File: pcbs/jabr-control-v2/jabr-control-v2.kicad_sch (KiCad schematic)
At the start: 4 parts

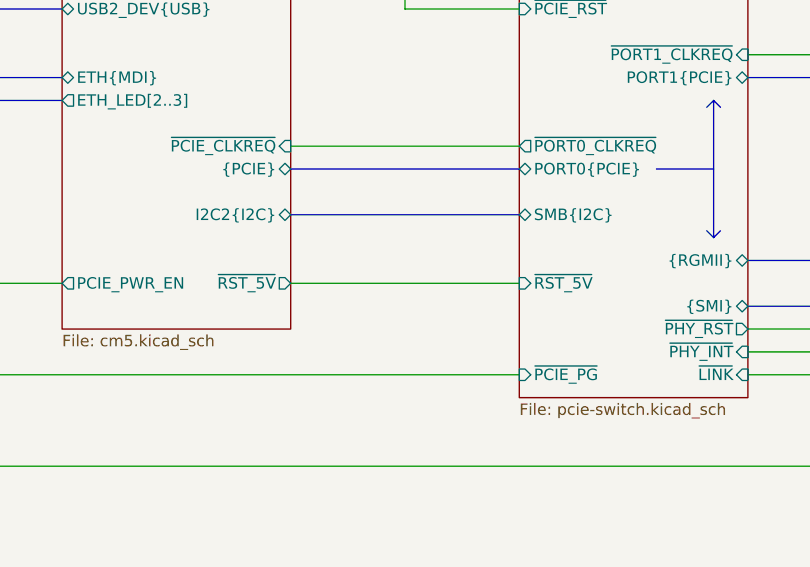
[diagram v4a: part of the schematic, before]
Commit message: Removed power button reset to switch (power will be cycled anyway)
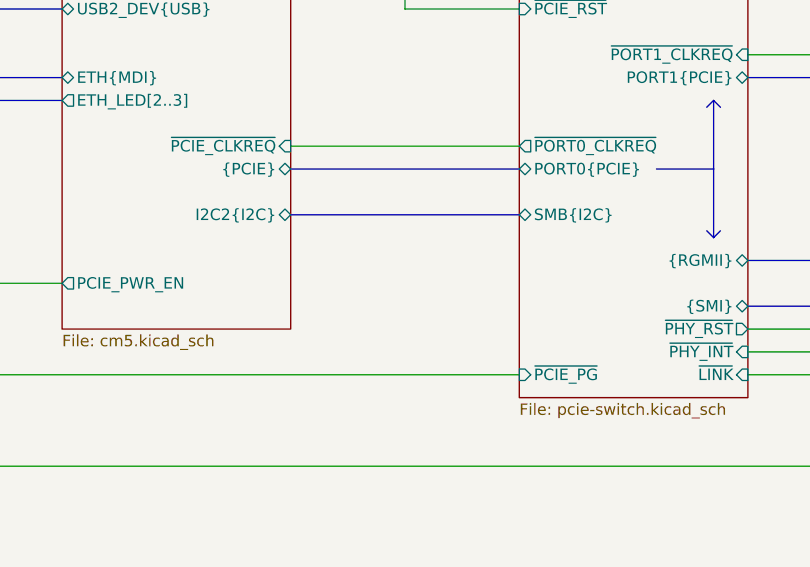
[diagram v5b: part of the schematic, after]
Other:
- sheet CM5 ports: added none; removed ~{RST_5V}
- sheet PCIe Switch ports: added none; removed ~{RST_5V}
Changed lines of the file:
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@@
-		)
-	)
-	(wire
-		(pts
-			(xy 139.7 129.54) (xy 165.1 129.54)
-		)
-		(stroke
-			(width 0)
-			(type default)
 		)
 	)
@@
 			)
 		)
-		(pin "~{RST_5V}" input
-			(at 165.1 129.54 180)
-			(effects
-				(font
-					(size 1.27 1.27)
-				)
-				(justify left)
-			)
-		)
 		(pin "~{PORT0_CLKREQ}" output
 			(at 165.1 114.3 180)
@@
 			)
 		)
-		(pin "~{RST_5V}" output
-			(at 139.7 129.54 0)
-			(effects
-				(font
-					(size 1.27 1.27)
-				)
-				(justify right)
-			)
-		)

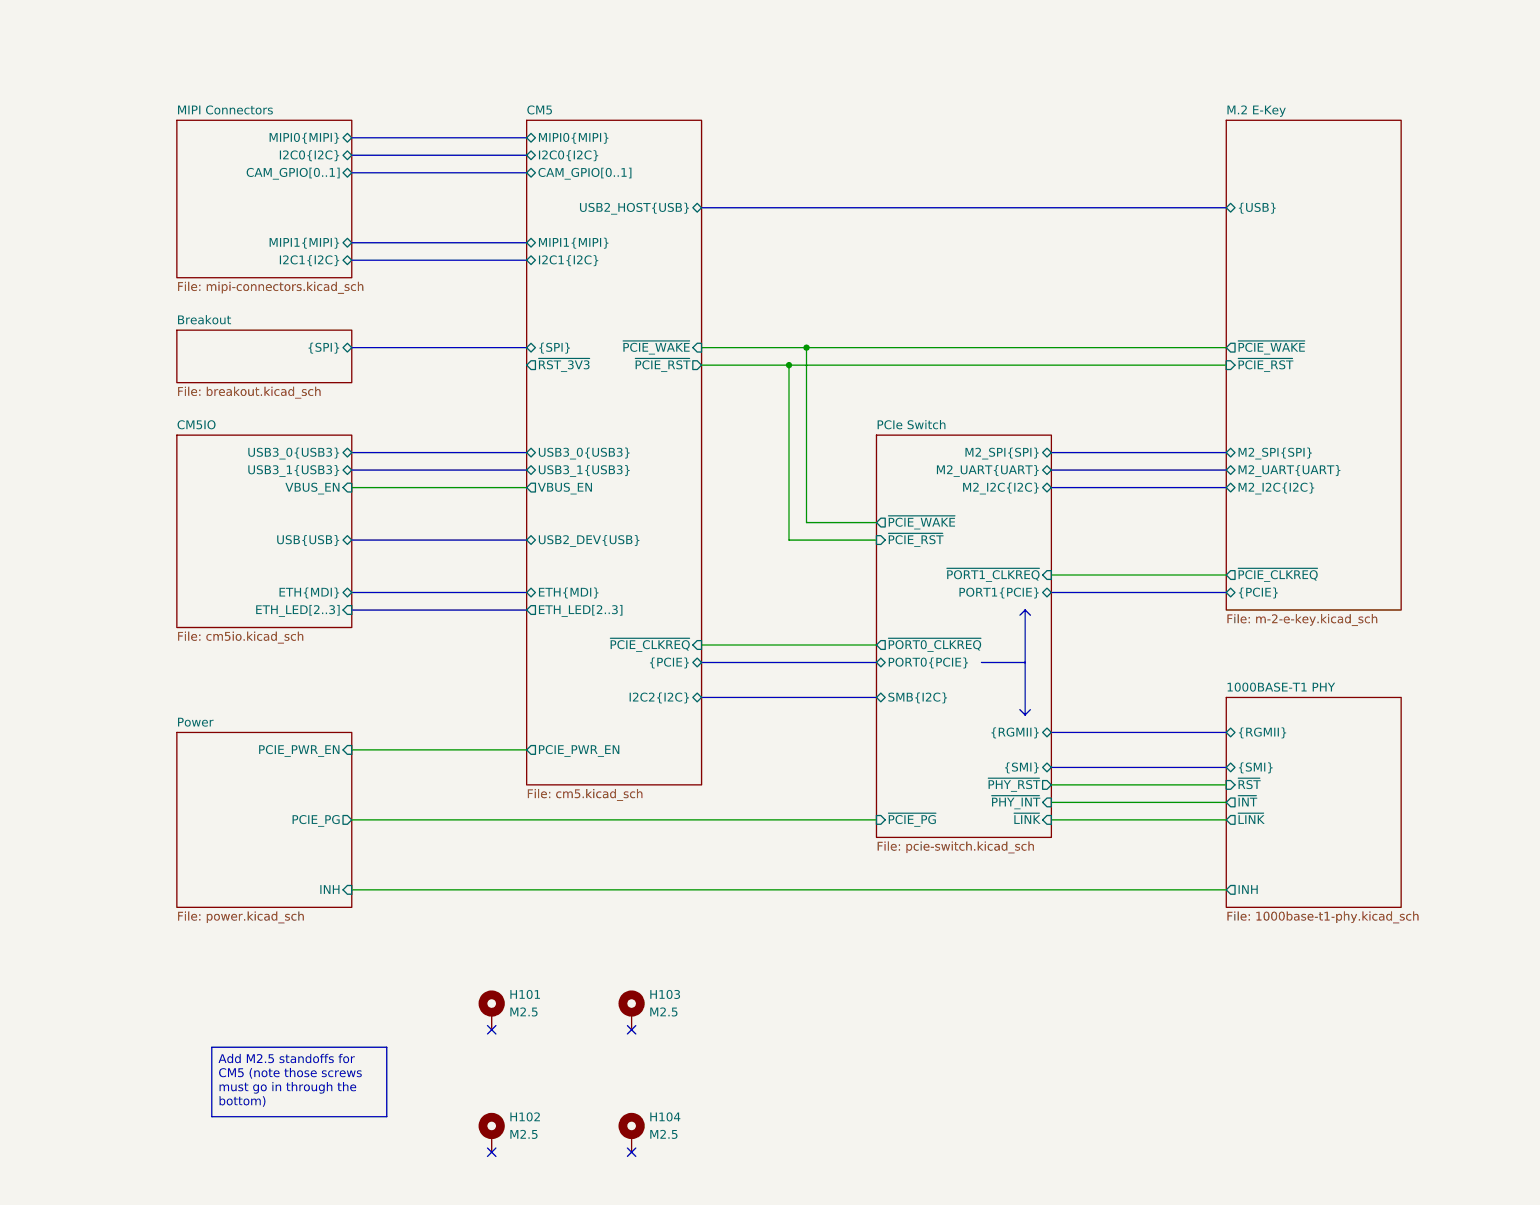
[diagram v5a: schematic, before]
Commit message: Schematic done
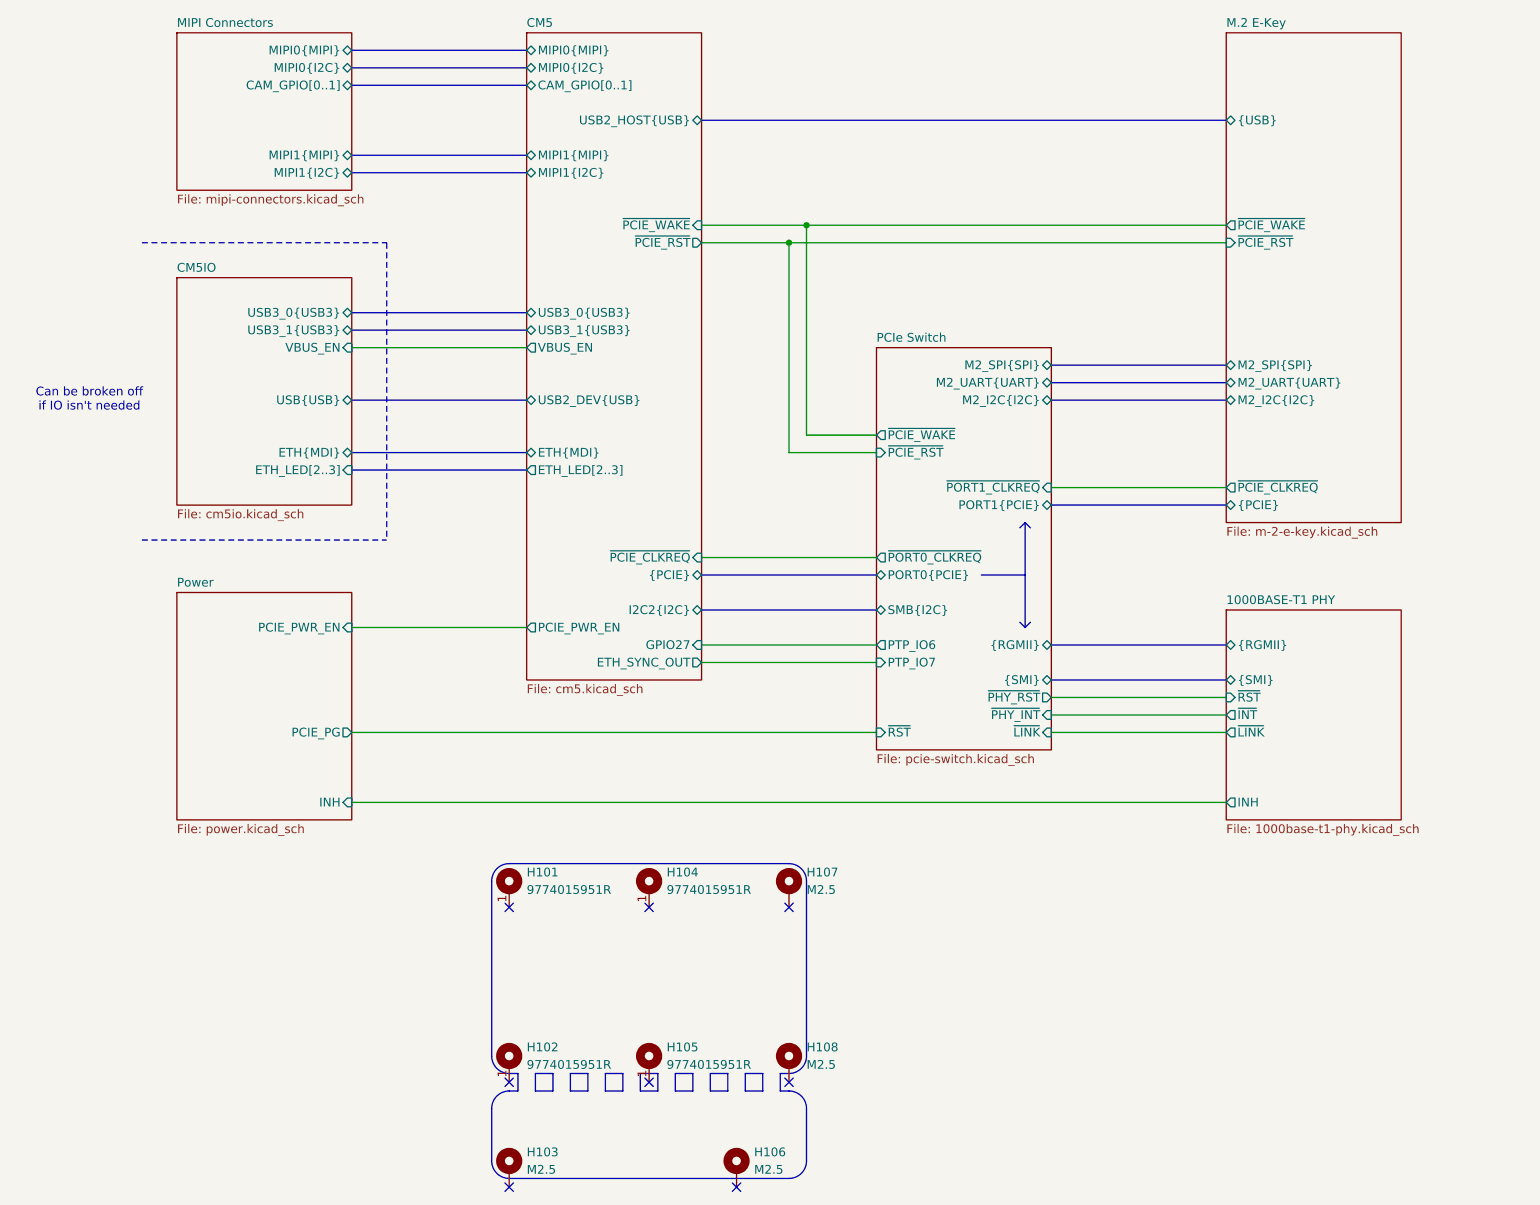
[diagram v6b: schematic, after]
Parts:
- added H101, H102, H104, H105: 9774015951R, Mounting_Wuerth:Mounting_Wuerth_WA-SMST-2.7mm_H1.5mm_9774015951, symbol STANDOFF:9774015951R
- renumbered H102 to H103, H104 to H106, H101 to H107, H103 to H108
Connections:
- no-connect marks 4 -> 8
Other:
- removed sheet Breakout
- sheet CM5 ports: added ETH_SYNC_OUT, GPIO27, MIPI0{I2C}, MIPI1{I2C}; removed I2C0{I2C}, I2C1{I2C}, {SPI}, ~{RST_3V3}
- sheet MIPI Connectors ports: added MIPI0{I2C}, MIPI1{I2C}; removed I2C0{I2C}, I2C1{I2C}
- sheet PCIe Switch ports: added PTP_IO6, PTP_IO7, ~{RST}; removed ~{PCIE_PG}
- note added: "Can be broken off if IO isn't needed"
- moved on the sheet: H103, H106, H107, H108
